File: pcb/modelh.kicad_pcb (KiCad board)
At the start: 2 copper layers, 150 x 38 mm, 47 parts, among them J1 USB_B, J2 Conn_01x16, J3 Conn_01x12, J4 Conn_01x04, J5 Conn_02x03_Odd_Even, J6 Conn_02x05_Odd_Even, SW1 SW_Push, U1 STM32F103C8Tx, U2 AMS1117-3.3, Y1 8MHz, Y2 32.768KHz

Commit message: WIP
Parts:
- removed D1: B5819W, Diode_SMD:D_SOD-123
- added R16: 0, Resistor_SMD:R_0805_2012Metric_Pad1.15x1.40mm_HandSolder, F.Cu at (84.3, 61.2)
- R7, R8, R9: value 120 -> 60; footprint Resistor_SMD:R_0603_1608Metric -> Resistor_SMD:R_0805_2012Metric
- moved R11 13.1 mm to (90.2, 61.0)
- moved LED2 0.75 mm to (102.3, 72.3)
- moved R2 0.75 mm to (105.5, 72.0)
- moved R9 0.65 mm to (190.8, 64.5)
- moved C7 0.50 mm to (111.0, 75.2)
- moved C8 0.50 mm to (113.5, 75.2)
- moved Y2 0.50 mm to (112.3, 72.0)
- moved C9 0.40 mm to (107.8, 75.3)
- moved R8 0.30 mm to (190.8, 62.5)
- moved C14 0.29 mm to (105.9, 69.2)
- moved C13 0.10 mm to (110.9, 56.7)
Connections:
- R11 pad 1: D- -> D+
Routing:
- net D-: track 32.6 -> 6.83 mm
- net D+: track 5.90 -> 15.8 mm
- net +5V: track 13.1 -> 21.5 mm
- net +3V3: track 233.5 -> 236.0 mm, vias 2 -> 3
- net SWDIO: track 40.1 -> 38.6 mm
- net Net-(J1-Pad1): track 4.02 -> 4.72 mm
- net STATUSLED: track 7.39 -> 7.97 mm
- net col6: track 27.6 -> 28.1 mm
- net GND: track 21.2 -> 21.0 mm, vias 12 -> 28

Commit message: WIP
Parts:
- moved R1 1.20 mm to (77.1, 59.7)
- moved C14 0.20 mm to (105.9, 69.4)
- moved C5 0.15 mm to (116.9, 75.8), turned to 180 degrees
- moved C6 0.10 mm to (116.9, 67.8), turned to 180 degrees
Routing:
- net GND: track 21.0 -> 26.8 mm, vias 28 -> 33
- net OSC8OUT: track 13.0 -> 10.5 mm
- net OSC8IN: track 15.5 -> 13.1 mm
- net +3V3: track 236.0 -> 234.5 mm

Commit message: WIP
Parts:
- J2: footprint Connector_PinHeader_2.54mm:PinHeader_1x16_P2.54mm_Vertical -> Connector_PinSocket_2.54mm:PinSocket_1x16_P2.54mm_Vertical
- J4: footprint Connector_PinHeader_2.54mm:PinHeader_1x04_P2.54mm_Vertical -> Connector_PinSocket_2.54mm:PinSocket_1x04_P2.54mm_Vertical
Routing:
- net OSC8IN: track 13.1 -> 15.6 mm
- net OSC8OUT: track 10.5 -> 13.0 mm

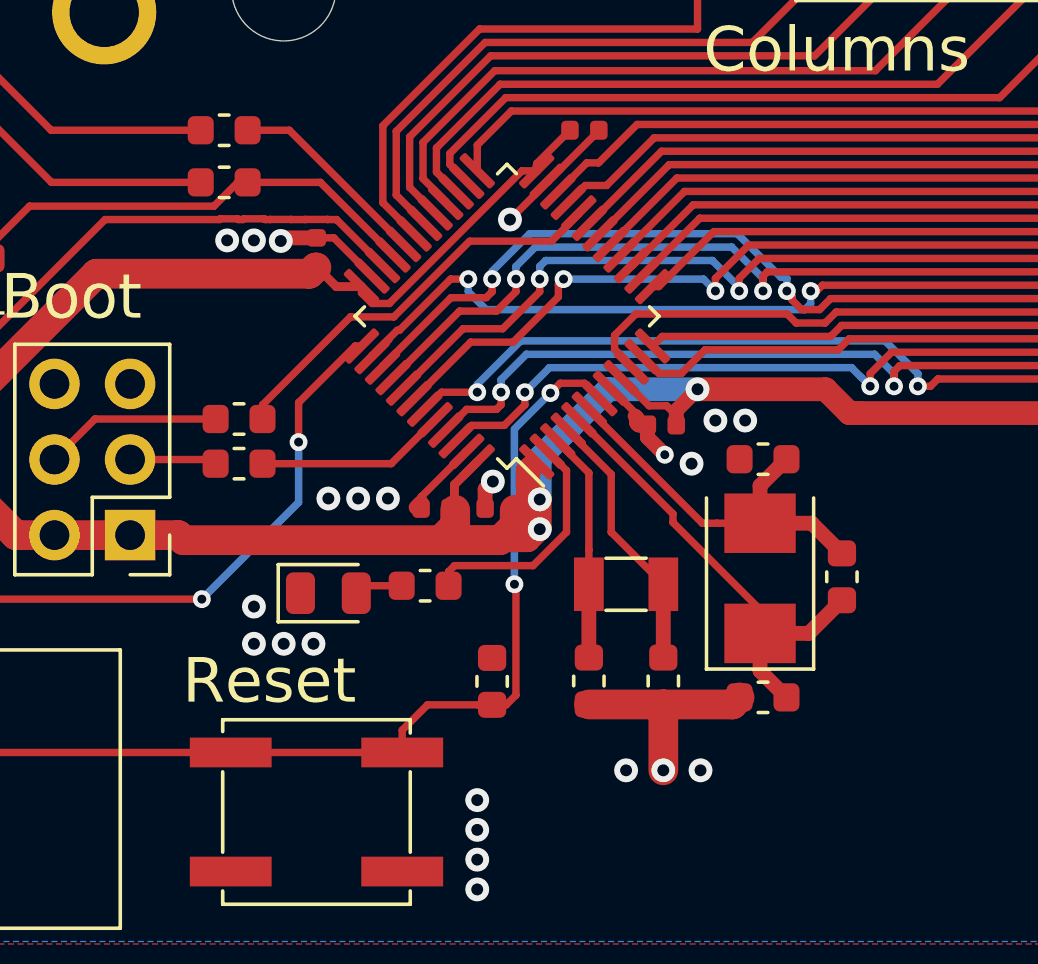
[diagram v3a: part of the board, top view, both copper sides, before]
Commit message: Remove LSE oscillator
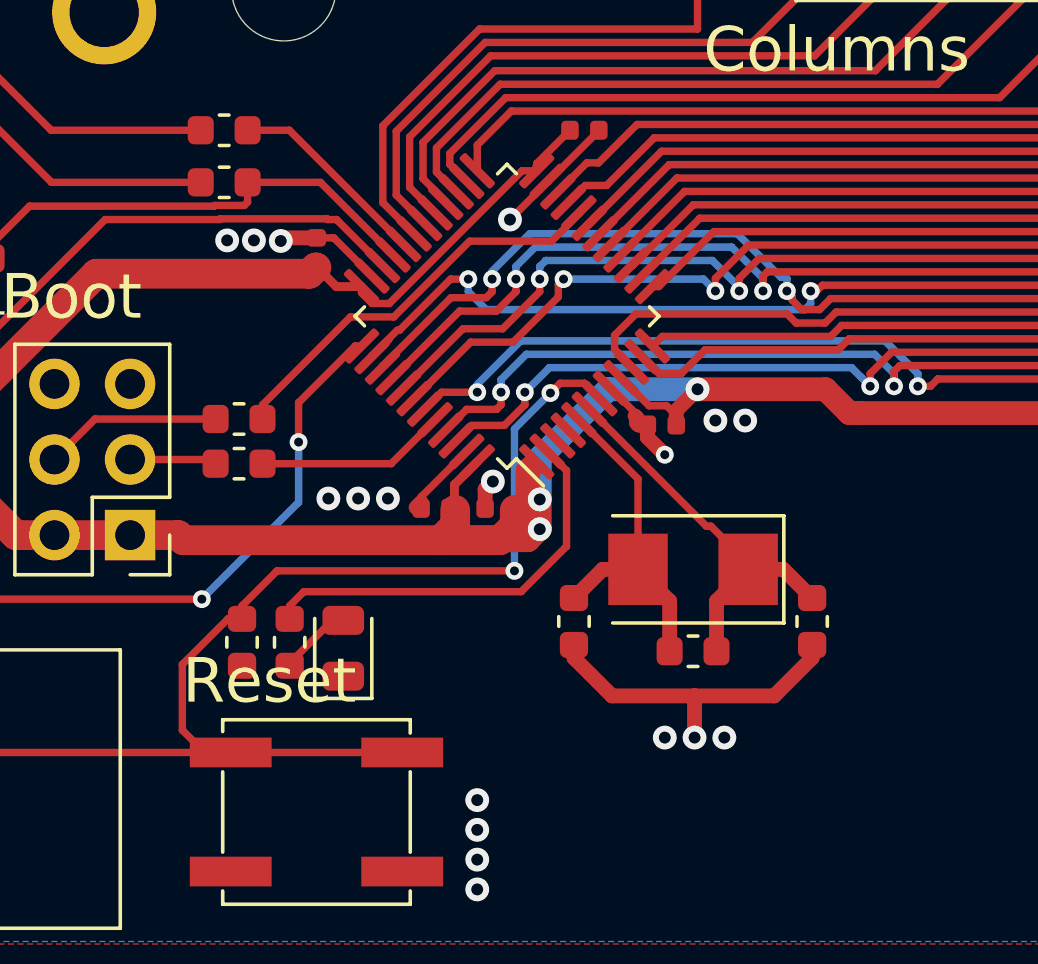
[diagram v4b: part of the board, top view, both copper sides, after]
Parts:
- removed C7, C8: 20pF, Capacitor_SMD:C_0603_1608Metric
- removed Y2: 32.768KHz, Crystal:Crystal_SMD_3215-2Pin_3.2x1.5mm
- moved C9 8.50 mm to (99.4, 73.9), turned to 270 degrees
- moved C6 8.37 mm to (110.5, 73.2), turned to 270 degrees
- moved R6 5.59 mm to (114.5, 74.2), turned to 180 degrees
- moved R2 4.93 mm to (101.0, 73.9), turned to 270 degrees
- moved C5 3.04 mm to (118.5, 73.2), turned to 270 degrees
- moved Y1 2.27 mm to (114.5, 71.5), turned to 180 degrees
- moved LED2 1.92 mm to (102.8, 74.1), turned to 90 degrees
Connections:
- U1 pad 3: OSC32IN -> (no net)
- U1 pad 4: OSC32OUT -> (no net)
- U1 pad 5: OSC8IN -> OSC8OUT
- U1 pad 6: OSC8OUT -> OSC8IN
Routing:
- net OSC32OUT: track 8.96 -> 0.00 mm
- net OSC32IN: track 7.71 -> 0.00 mm
- net nRST: track 32.8 -> 40.4 mm
- net STATUSLED: track 7.97 -> 14.0 mm
- net GND: track 26.8 -> 30.8 mm, vias 33 -> 28
- net OSC8IN: track 15.6 -> 13.4 mm
- net OSC8OUT: track 13.0 -> 11.6 mm
- net Net-(LED2-Pad2): track 1.28 -> 2.48 mm

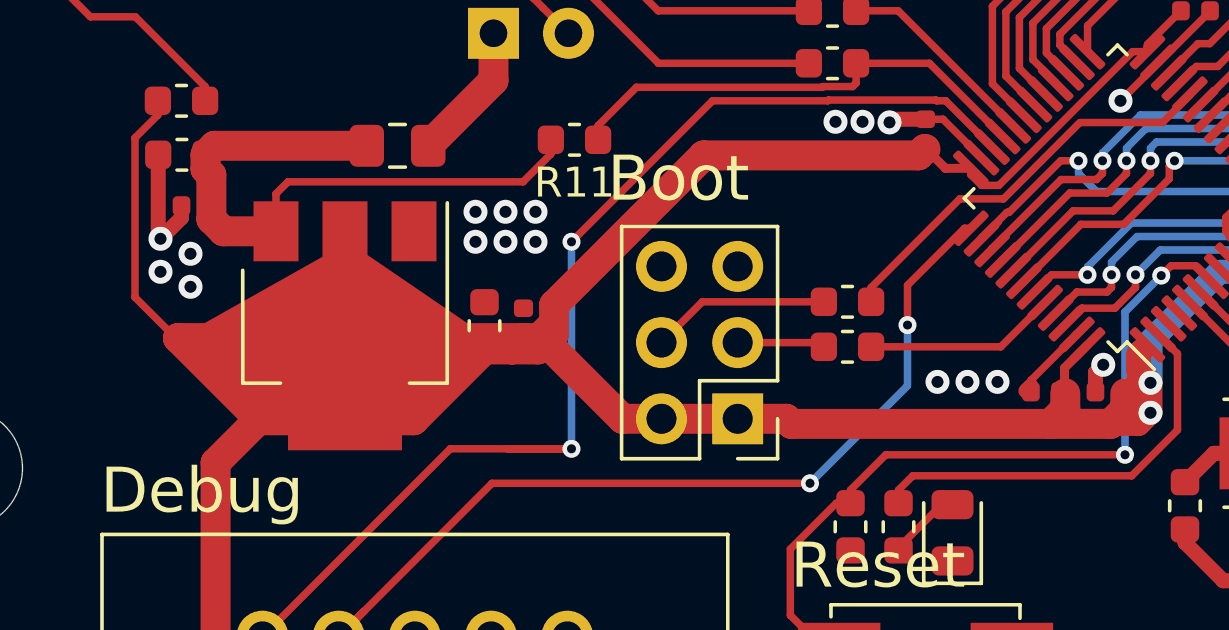
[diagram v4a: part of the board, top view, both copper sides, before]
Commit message: Make boot selection pins optional
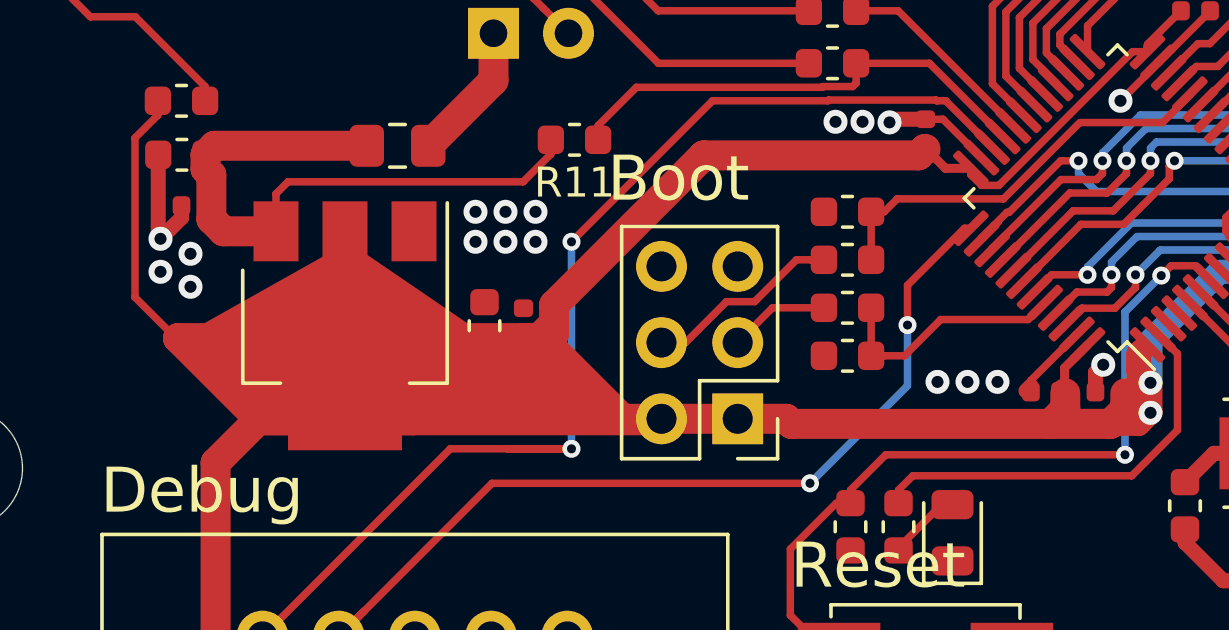
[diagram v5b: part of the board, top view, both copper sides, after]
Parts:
- added R17: 100k, Resistor_SMD:R_0603_1608Metric, F.Cu at (99.3, 68.2)
- added R18: 100k, Resistor_SMD:R_0603_1608Metric, F.Cu at (99.3, 63.4)
- LED1: value LED -> green
- LED2: value LED -> amber
- R10, R5: value 100k -> 1k
- moved R10 1.40 mm to (99.3, 65.0)
- moved R5 1.30 mm to (99.3, 66.6)
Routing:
- net BOOT0: track 6.41 -> 8.14 mm
- net Net-(J5-Pad4): track 5.98 -> 6.56 mm

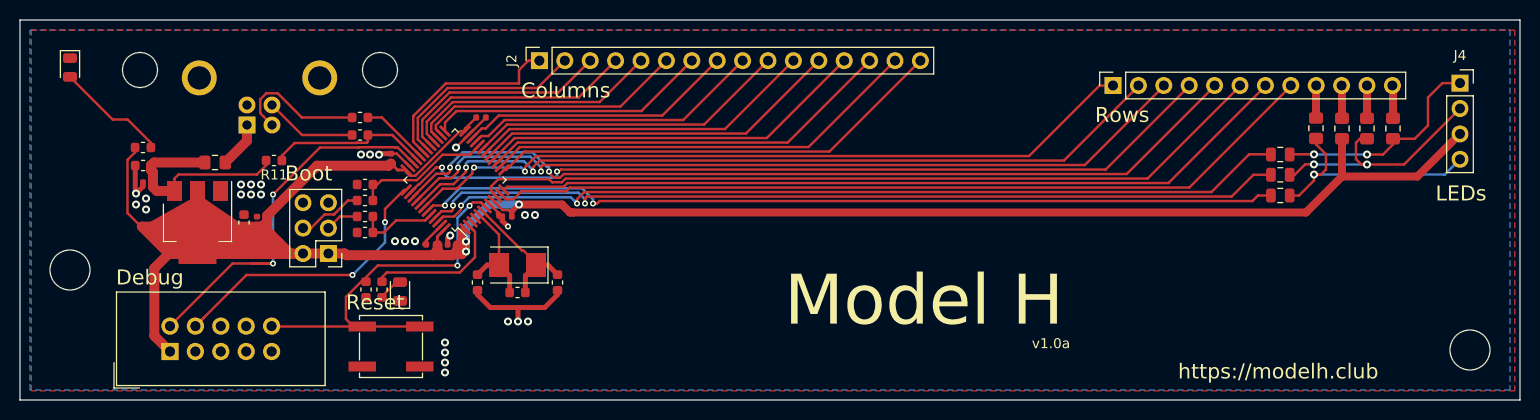
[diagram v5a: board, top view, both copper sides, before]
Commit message: Create testpoints for custom LEDs
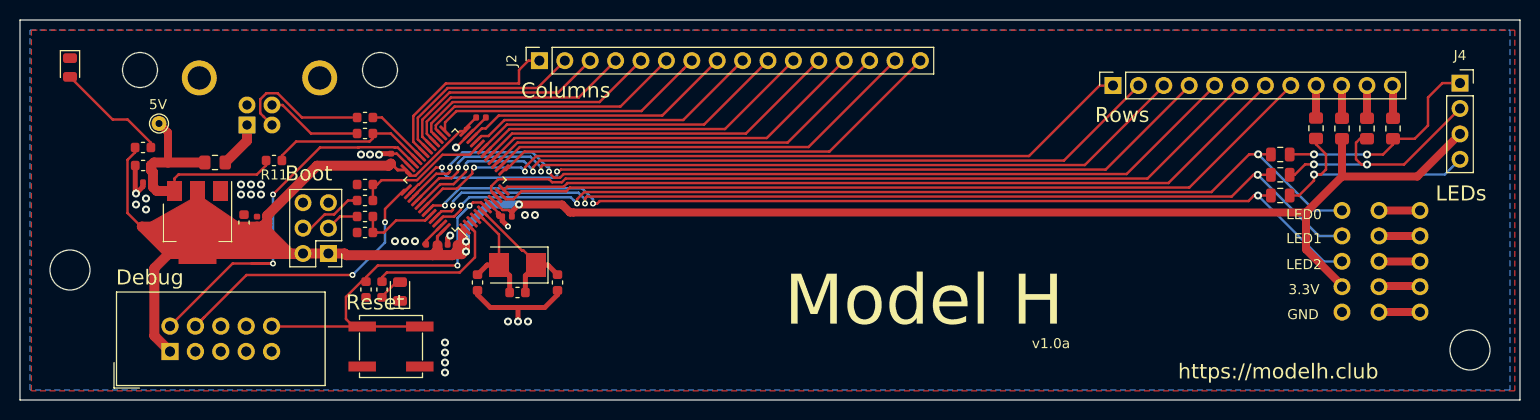
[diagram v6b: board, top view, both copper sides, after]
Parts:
- added J7: Conn_01x05, Connector_PinSocket_2.54mm:Conn_Generic_01x05, F.Cu at (204.8, 66.0)
- added J8: Conn_01x05, Connector_PinSocket_2.54mm:Conn_Generic_01x05, F.Cu at (197.0, 66.0)
- added J9: Conn_01x05, Connector_PinSocket_2.54mm:Conn_Generic_01x05, F.Cu at (200.7, 66.0)
- added TP1: TestPoint, TestPoint:TestPoint_THTPad_D1.5mm_Drill0.7mm, F.Cu at (78.7, 57.3)
- moved R3 0.52 mm to (99.3, 58.3)
- moved R4 0.50 mm to (99.3, 56.7)
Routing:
- net led2: track 86.8 -> 98.0 mm, vias 2 -> 3
- net led1: track 87.4 -> 98.4 mm, vias 2 -> 3
- net led0: track 87.3 -> 98.0 mm, vias 2 -> 3
- net +3V3: track 234.5 -> 243.4 mm
- net +5V: track 21.5 -> 25.8 mm
- net Net-(J7-Pad4): track 0.00 -> 4.13 mm
- net Net-(J7-Pad3): track 0.00 -> 4.12 mm
- net Net-(J7-Pad5): track 0.00 -> 4.11 mm
- net Net-(J7-Pad1): track 0.00 -> 4.11 mm
- net Net-(J7-Pad2): track 0.00 -> 4.10 mm
- net D-: track 6.83 -> 6.33 mm
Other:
- board text added: "3.3V"
- board text added: "5V"
- board text added: "GND"
- board text added: "LED0"
- board text added: "LED1"
- board text added: "LED2"
